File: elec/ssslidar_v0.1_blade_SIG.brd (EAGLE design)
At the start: 12.5 x 5 mm, 22 parts, among them P1 PIN_SMD_0.8X1_RECT, P10 PIN_SMD_0.8X1_RECT, P11 PIN_SMD_1X1_RECT, P12 PIN_SMD_0.8X1_RECT, P13 PIN_SMD_0.8X1_RECT, P16 PIN_SMD_0.8X1_RECT, P17 PIN_SMD_1X1_RECT, P18 PIN_SMD_0.8X1_RECT, P2 PIN_SMD_1X1_RECT, P3 PIN_SMD_0.8X1_RECT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

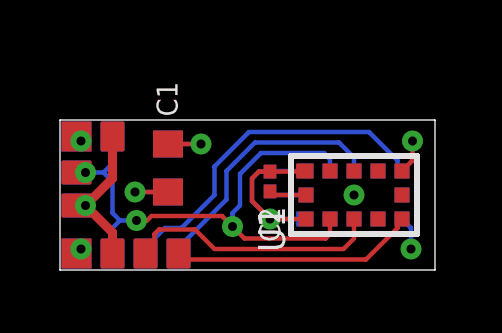
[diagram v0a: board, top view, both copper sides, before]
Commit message: Added SIG blade.
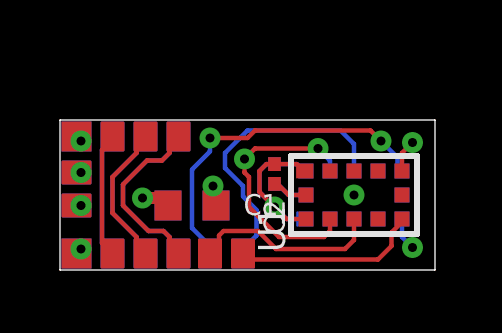
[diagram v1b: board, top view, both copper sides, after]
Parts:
- added P14, P15, P19, P20, P21, P22, P23, P24: PIN_SMD_0.8X1_RECT, Xevelabs:PIN_SMD_0.8X1_RECT
- moved P18 4.48 mm to (3.95, 0.55), turned to 270 degrees
- moved P3 3.90 mm to (1.75, 4.45), turned to 270 degrees
- moved P1 2.20 mm to (3.95, 4.45), flipped to the bottom, turned to 270 degrees
- moved P4 2.15 mm to (5.00, 0.55)
- moved P7 2.15 mm to (5.00, 0.55)
- moved P5 2.15 mm to (6.10, 0.55)
- moved P6 2.15 mm to (6.10, 0.55)
- moved C1 1.48 mm to (4.40, 2.15), turned to 0 degrees
- moved C3 1.48 mm to (4.40, 2.15), turned to 180 degrees
- moved P8 1.10 mm to (2.85, 0.55), flipped to the bottom, turned to 270 degrees
- moved C2 0.29 mm to (7.15, 3.20)
- moved C4 0.29 mm to (7.15, 3.20)
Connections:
- new net N$1: P14.PIN, P20.PIN
- new net N$2: P15.PIN, P21.PIN
- new net N$3: P19.PIN, P22.PIN
- new net N$4: P1.PIN, P18.PIN
- new net N$5: P23.PIN, P3.PIN
- new net N$6: P24.PIN, P8.PIN
- net SCL: no longer P18.PIN, P3.PIN
- net VDD: no longer P1.PIN, P8.PIN
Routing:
- net N$3: track 0.00 -> 6.02 mm
- net N$4: track 0.00 -> 6.02 mm
- net VDD: track 19.0 -> 13.1 mm
- net N$6: track 0.00 -> 4.81 mm
- net N$2: track 0.00 -> 4.81 mm
- net SCL: track 19.1 -> 14.7 mm
- net N$5: track 0.00 -> 4.19 mm
- net N$1: track 0.00 -> 4.19 mm
- net SDA1: track 8.55 -> 6.36 mm
- net INT1: track 8.18 -> 6.26 mm
- net SDA2: track 8.71 -> 9.67 mm
- net GND: track 5.55 -> 4.64 mm
- net INT2: vias 0 -> 2

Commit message: Working on main board Made blades longer to avoid too much occlusion from the main PCB (but we will still need to put the whole thing on a mast).
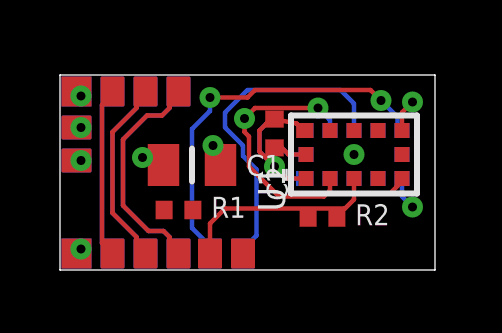
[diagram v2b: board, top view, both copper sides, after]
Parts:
- removed C3: 4.7uF, Xevelabs:0603_N
- removed C4: 100nF, Xevelabs:0201_N
- added R1, R2: (no value), Xevelabs:0402_N
- C1: value 4.7uF -> 10uF; device Xevelabs:0603_N -> Xevelabs:0805_N
- C2: device Xevelabs:0201_N -> Xevelabs:0402_N
- moved P1 1.50 mm to (3.95, 5.95)
- moved P10 1.50 mm to (0.55, 4.75)
- moved P12 1.50 mm to (0.55, 4.75)
- moved P13 1.50 mm to (0.55, 3.65)
- moved P14 1.50 mm to (1.75, 5.95)
- moved P16 1.50 mm to (0.55, 3.65)
- moved P2 1.50 mm to (0.55, 5.95)
- moved P21 1.50 mm to (2.85, 5.95)
- moved P22 1.50 mm to (3.95, 5.95)
- moved P24 1.50 mm to (2.85, 5.95)
- moved P3 1.50 mm to (1.75, 5.95)
- moved P9 1.50 mm to (0.55, 5.95)
- moved C1 1.35 mm to (4.40, 3.50)
- moved U1 1.35 mm to (9.80, 3.85)
- moved U2 1.35 mm to (9.80, 3.85)
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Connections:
- net GND: no longer C3.2, C4.2
- net SDA1: now also R2.1
- net SDA2: now also R1.1
- net VDD: now also R1.2, R2.2; no longer C3.1, C4.1
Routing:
- net INT1: track 6.26 -> 0.59 mm
- net N$4: track 6.02 -> 7.52 mm
- net N$5: track 4.19 -> 5.69 mm
- net N$1: track 4.19 -> 5.69 mm
- net N$6: track 4.81 -> 6.31 mm
- net N$3: track 6.02 -> 7.52 mm
- net N$2: track 4.81 -> 6.31 mm
- net VDD: track 13.1 -> 11.6 mm
- net SDA2: track 9.67 -> 11.0 mm
- net INT2: track 11.6 -> 12.9 mm
- net SDA1: track 6.36 -> 7.26 mm
- net GND: track 4.64 -> 4.09 mm
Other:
- board size 12.5 x 5 mm -> 12.5 x 6.5 mm

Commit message: Updated blades (ready for release). Double power rail for sensors.
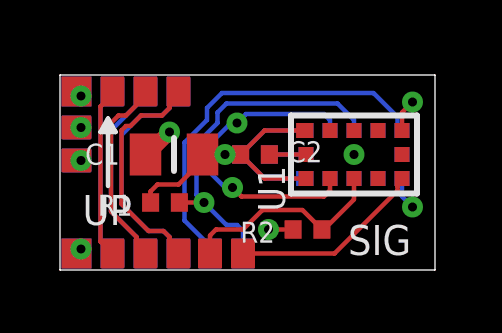
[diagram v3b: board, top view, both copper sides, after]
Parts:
- added C3: 100nF, Xevelabs:0402_N
- R1, R2: value (none) -> 2k
- moved C2 0.96 mm to (6.50, 3.85), turned to 0 degrees
- moved C1 0.69 mm to (3.80, 3.85), turned to 180 degrees
- moved R2 0.64 mm to (8.25, 1.35), turned to 180 degrees
- moved R1 0.51 mm to (3.50, 2.25), turned to 180 degrees
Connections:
- net GND: now also C3.2
- net VDD: now also C3.1
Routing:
- net VDD: track 11.6 -> 17.8 mm
- net INT1: track 0.59 -> 6.48 mm
- net SCL: track 14.6 -> 16.6 mm
- net SDA2: track 11.0 -> 12.1 mm, vias 0 -> 1
- net INT2: vias 2 -> 0
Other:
- board text added: "SIG"
- board text added: "UP"

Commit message: Made blades slightly taller (7mm instead of 6.5)
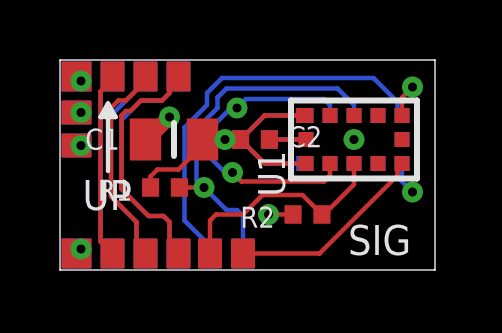
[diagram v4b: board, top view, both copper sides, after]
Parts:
- moved P13 0.50 mm to (0.55, 4.15)
- moved P16 0.50 mm to (0.55, 4.15)
- moved P1 0.50 mm to (3.95, 6.45)
- moved P10 0.50 mm to (0.55, 5.25)
- moved P12 0.50 mm to (0.55, 5.25)
- moved P14 0.50 mm to (1.75, 6.45)
- moved P2 0.50 mm to (0.55, 6.45)
- moved P21 0.50 mm to (2.85, 6.45)
- moved P22 0.50 mm to (3.95, 6.45)
- moved P24 0.50 mm to (2.85, 6.45)
- moved P3 0.50 mm to (1.75, 6.45)
- moved P9 0.50 mm to (0.55, 6.45)
- moved R1 0.50 mm to (3.50, 2.75)
- moved R2 0.50 mm to (8.25, 1.85)
- moved C1 0.50 mm to (3.80, 4.35)
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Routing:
- net N$4: track 7.68 -> 8.18 mm
- net SDA1: track 7.56 -> 8.06 mm
- net SDA2: track 12.1 -> 12.6 mm
- net N$6: track 6.35 -> 6.85 mm
- net N$5: track 5.73 -> 6.23 mm
- net N$3: track 7.76 -> 8.26 mm
- net N$2: track 6.50 -> 7.00 mm
- net N$1: track 5.73 -> 6.23 mm
- net INT2: track 12.9 -> 13.4 mm
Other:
- board size 12.5 x 6.5 mm -> 12.5 x 7 mm

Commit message: Routing done.
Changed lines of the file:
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@@
 <layer number="97" name="Info" color="7" fill="1" visible="no" active="no"/>
 <layer number="98" name="Guide" color="6" fill="1" visible="no" active="no"/>
+<layer number="99" name="SpiceOrder" color="5" fill="1" visible="no" active="no"/>
 <layer number="100" name="Muster" color="7" fill="1" visible="no" active="no"/>
 <layer number="101" name="Patch_Top" color="12" fill="4" visible="no" active="yes"/>
@@
 <text x="9.6" y="0.5" size="1" layer="21" font="vector" ratio="15">SIG</text>
 <text x="11.85" y="0.5" size="1" layer="22" font="vector" ratio="15" rot="MR0">SIG</text>
+<circle x="8.15" y="6.15" radius="0.25" width="0" layer="21"/>
+<circle x="8.15" y="2.5" radius="0.25" width="0" layer="22"/>
 </plain>
 <attributes>
